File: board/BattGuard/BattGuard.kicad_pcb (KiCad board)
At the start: 4 copper layers, 160 x 80 mm, 160 parts, among them J1 OQ0271510000G, J10 Conn_01x01_Pin, J11 Conn_01x01_Pin, J12 Conn_01x01_Pin, J13 Conn_01x01_Pin, J15 Conn_01x01_Pin, J17 S5B-XH-A, J18 FAN1 5V, J19 FAN2 5V, J2 Barrel_Jack, J3 Conn_01x22_Pin, J4 Conn_01x22_Pin, J5 Conn_01x02_Pin(xt60), J6 OLED DISPLAY, J8 GSB4111312HR, J9 Conn_01x01_Pin, Q1 SIR680LDP-T1-RE3, Q2 SIR680LDP-T1-RE3, Q3 SIR680LDP-T1-RE3, Q4 SIR680LDP-T1-RE3, Q5 Q_PMOS_DGS, Q7 AO3401A, Q8 2N7002, SW1 SW_Push, SW2 SW_Push, U1 BQ25756ERRVR, U2 LMR51420XDDCR, U3 MCP45HV51-ST, U4 INA226, U5 LM317_TO3, U6 TLV76133KVUR, U7 TLV61047DDC

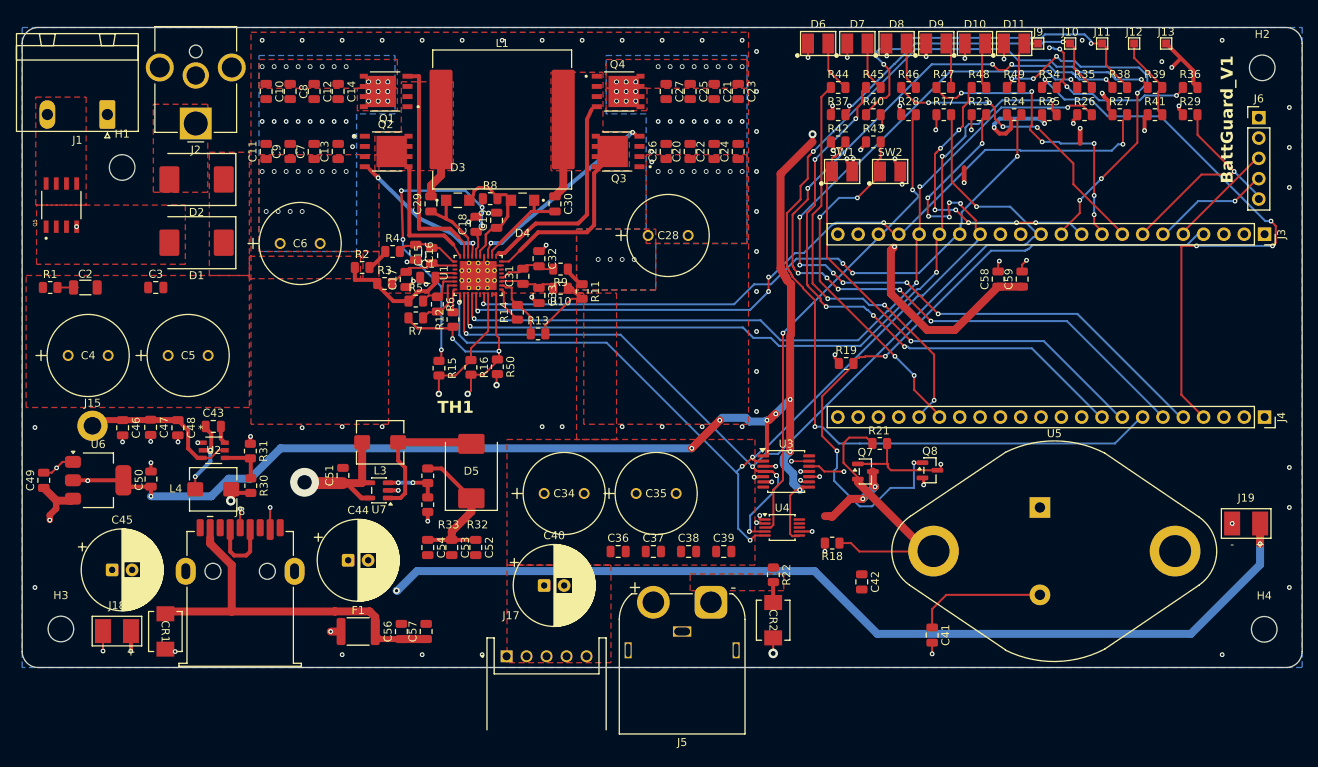
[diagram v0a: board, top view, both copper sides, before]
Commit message: 10.30.2026 updated
updated capicator footprints, cleaned up and routed 12v charge circuit section, updated clearance rules for pad clearnce issues.
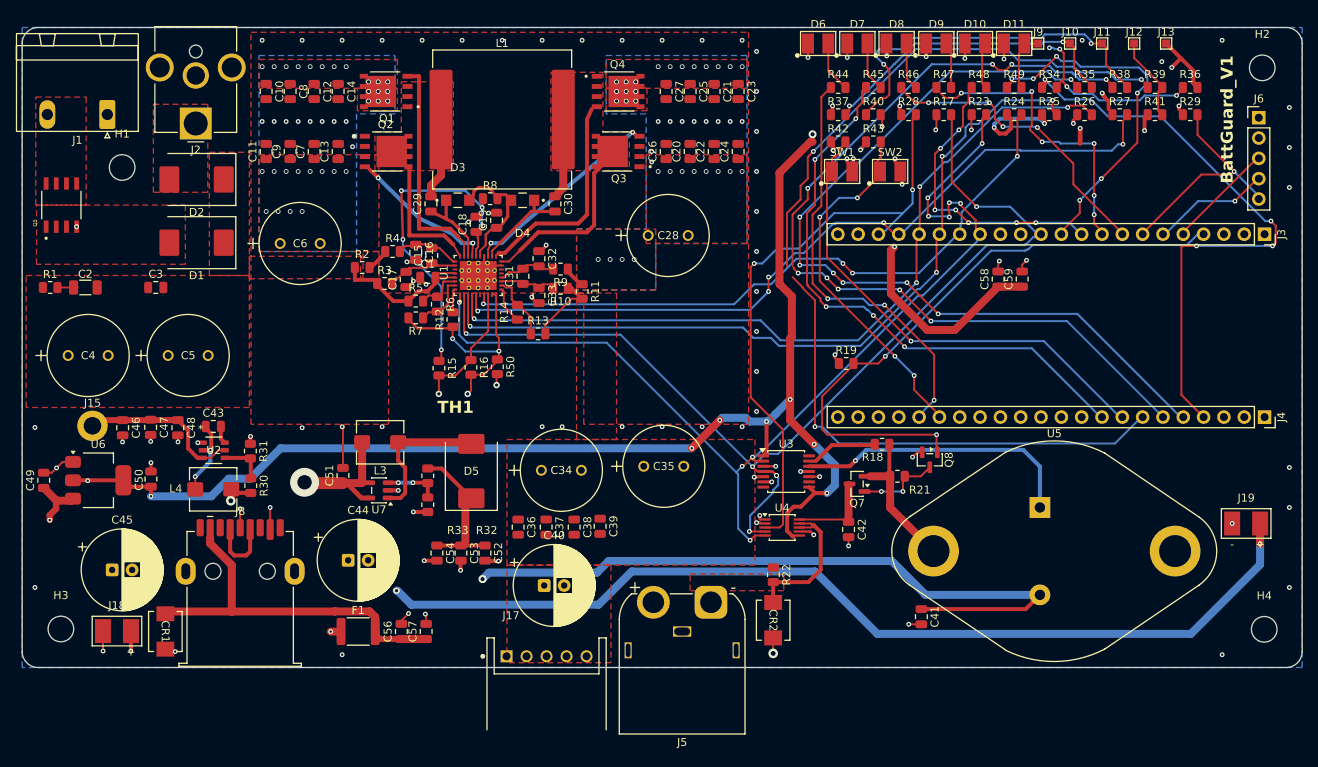
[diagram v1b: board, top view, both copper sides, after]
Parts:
- moved C39 15.8 mm to (172.2, 112.3), turned to -90 degrees
- moved C38 14.6 mm to (169.0, 112.5), turned to -90 degrees
- moved R18 13.8 mm to (207.5, 102.1)
- moved C37 13.7 mm to (165.5, 112.5), turned to -90 degrees
- moved C36 12.9 mm to (162.0, 112.5), turned to -90 degrees
- moved C42 6.75 mm to (203.3, 112.8)
- moved R21 4.66 mm to (209.4, 106.1)
- moved C35 3.53 mm to (177.7, 104.8)
- moved C34 2.92 mm to (164.9, 105.3)
- moved C41 2.67 mm to (212.4, 123.7)
- moved Q7 1.87 mm to (204.4, 107.0), turned to 180 degrees
- moved C52 1.35 mm to (157.8, 115.7)
- moved C53 1.35 mm to (154.8, 115.7)
- moved C54 1.35 mm to (151.8, 115.7)
- moved Q8 1.31 mm to (213.4, 104.0), turned to -90 degrees
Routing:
- net /+18.5V: track 35.7 -> 106.2 mm, vias 0 -> 1
- net +BATT: track 4.37 -> 20.6 mm
- net /GPIO14: track 58.3 -> 74.3 mm
- net Net-(Q7-S): track 64.9 -> 49.6 mm
- net GND: track 55.3 -> 68.0 mm, vias 117 -> 120
- net Net-(U3-P0A): track 17.5 -> 9.10 mm, vias 2 -> 0
- net Net-(Q7-G): track 16.1 -> 9.68 mm, vias 1 -> 2
- net +3V3: track 190.0 -> 195.9 mm, vias 24 -> 23
- net /GPIO4: track 82.4 -> 77.1 mm, vias 3 -> 2
- net /Vsystem: track 113.0 -> 109.1 mm
- net /GPIO41: track 128.7 -> 127.2 mm
- net +5V: track 164.2 -> 165.6 mm
- net Net-(Q7-D): track 9.84 -> 11.1 mm, vias 2 -> 0

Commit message: 10.30.2026 fixed capictor routing, 18.5 feed line setup correctly 12v charge circuit done and cleaned up
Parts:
- moved C58 26.2 mm to (243.5, 66.5), turned to -90 degrees
- moved C59 21.6 mm to (240.5, 66.5), turned to -90 degrees
- moved C42 5.71 mm to (203.0, 118.5)
- moved C36 0.81 mm to (162.8, 112.3)
- moved C37 0.81 mm to (166.3, 112.3)
- moved C38 0.81 mm to (169.8, 112.3)
- moved C39 0.81 mm to (173.1, 112.2)
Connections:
- C58 pad 1: +5V -> +3V3
- C59 pad 1: +5V -> +3V3
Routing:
- net +5V: track 165.6 -> 139.2 mm, vias 7 -> 6
- net Net-(Q7-D): track 11.1 -> 26.8 mm
- net /+18.5V: track 106.2 -> 118.2 mm, vias 1 -> 8
- net GND: track 68.0 -> 78.6 mm, vias 120 -> 125
- net /GPIO9: track 127.4 -> 121.9 mm, vias 10 -> 6
- net +3V3: track 195.9 -> 200.4 mm, vias 23 -> 25
- net +BATT: track 20.6 -> 22.6 mm, vias 0 -> 1
- net Net-(J9-Pin_1): track 23.3 -> 25.3 mm, vias 4 -> 2
- net /GPIO41: track 127.2 -> 128.7 mm
- added copper zone on F.Cu, net /+18.5V

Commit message: 10.30.2026 rev 1
all traces routed, time to go through shivams checklist
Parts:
- R50: value 0 -> NetTie; footprint Resistor_SMD:R_0805_2012Metric -> TeamLib:NetTie_AGND_EP
- moved R50 9.48 mm to (158.8, 83.0), turned to 0 degrees
- moved C29 1.05 mm to (151.1, 73.1)
- moved C30 0.81 mm to (166.7, 72.8), turned to 180 degrees
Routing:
- net /SW1: track 29.2 -> 38.2 mm, vias 0 -> 2
- net /SW2: track 33.7 -> 42.3 mm, vias 0 -> 2
- net /LODRV2: track 24.9 -> 29.6 mm
- net Net-(U1-DRV_SUP): track 10.3 -> 14.5 mm
- net Net-(U1-SRN): track 4.99 -> 6.88 mm
- net GND: track 78.6 -> 77.1 mm, vias 125 -> 124
- net /LODRV1: track 18.0 -> 19.2 mm
- net /REGN: track 40.3 -> 41.1 mm
- net /BTST2: track 12.0 -> 11.4 mm
- net /HIDRV2: vias 0 -> 2
- net /HIDRV1: vias 0 -> 2

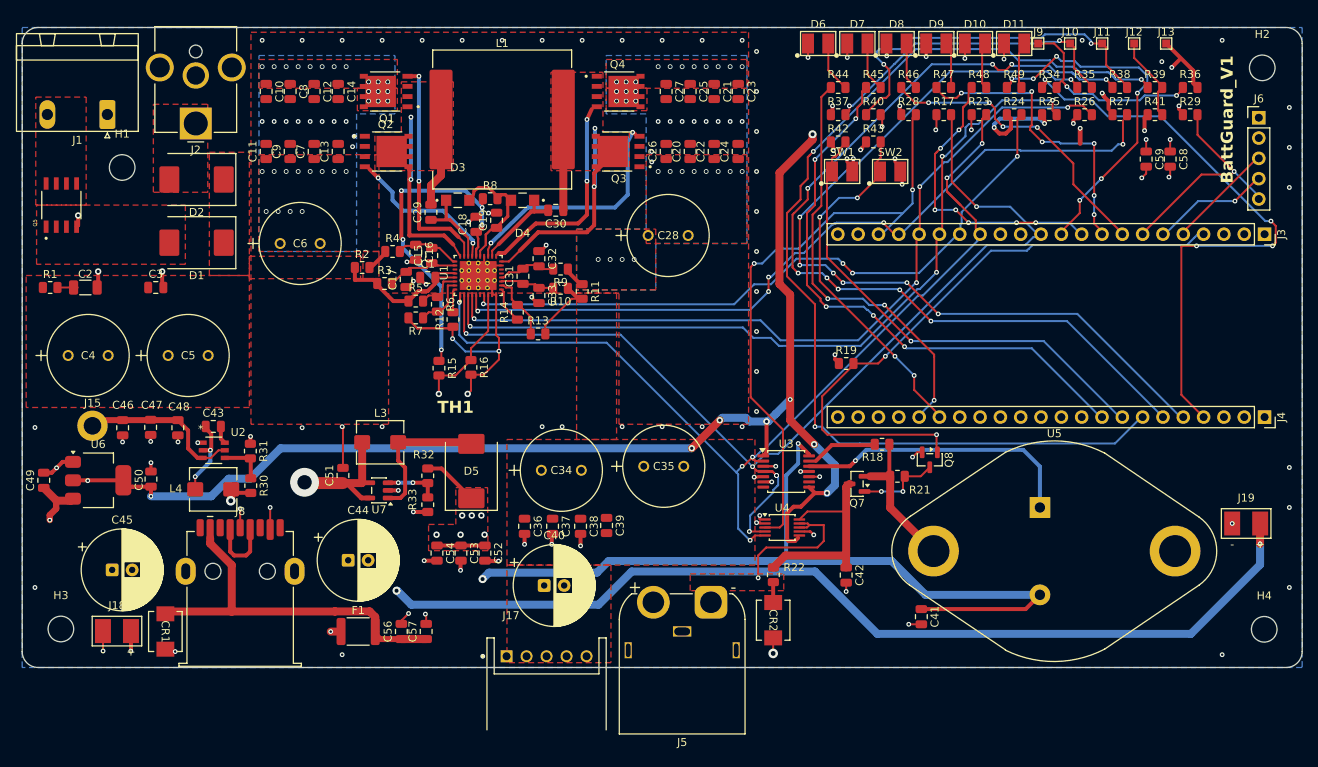
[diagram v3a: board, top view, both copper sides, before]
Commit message: Trace Cleaning/Straigtening SilkScreen Placement and Sizing
Throughout most of the board trace routing has been straightened out where possible. Silkscreen that overlapped in tight areas were resized, and most IC silkscreens labels were moved to nearby its Pin 1.
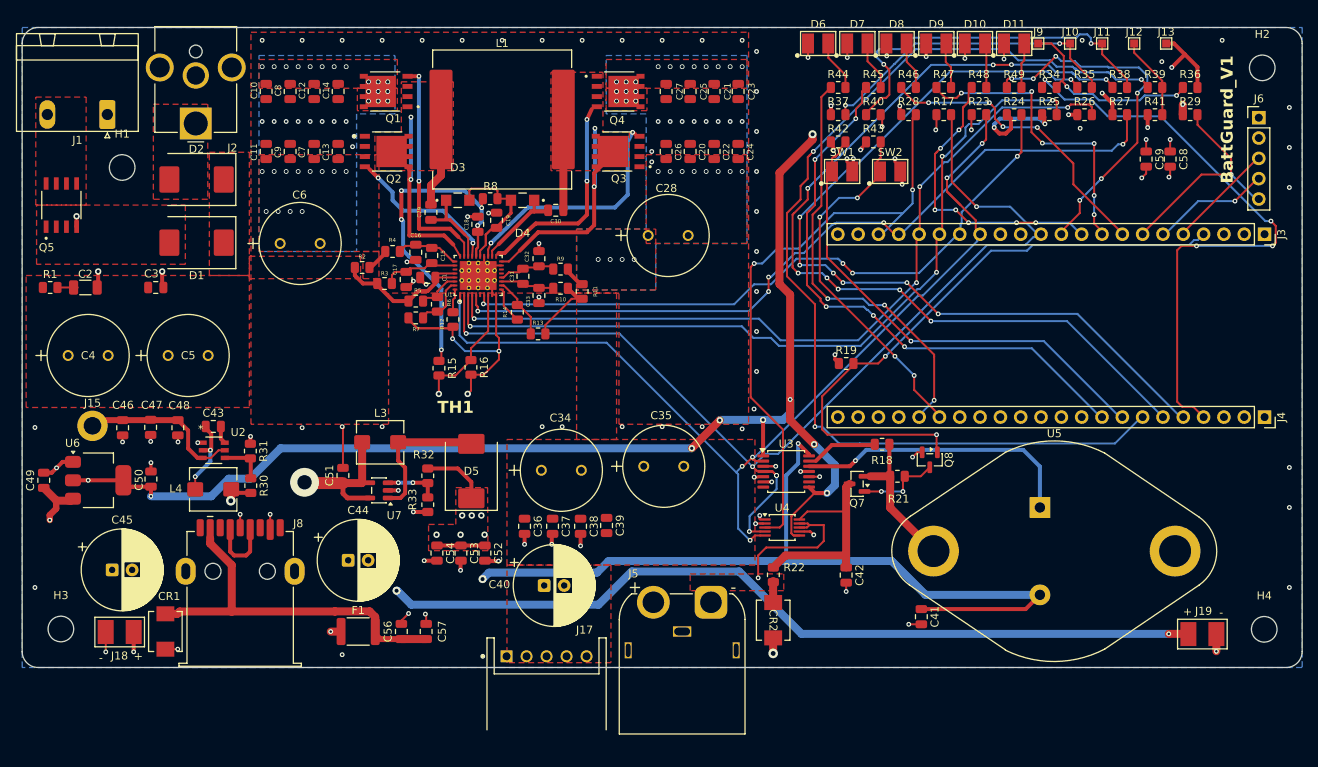
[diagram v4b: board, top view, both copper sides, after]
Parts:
- moved J19 14.9 mm to (247.5, 125.8), turned to 0 degrees
- moved J18 0.36 mm to (112.2, 125.6)
- moved C18 0.20 mm to (156.9, 74.6)
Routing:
- net +5V: track 139.2 -> 123.0 mm
- net +3V3: track 200.2 -> 203.8 mm
- net Net-(U1-ACP): track 7.34 -> 9.81 mm
- net Net-(U1-DRV_SUP): track 14.5 -> 15.8 mm
- net /GPIO13: track 95.6 -> 96.8 mm
- net Net-(D11-A): track 4.43 -> 5.65 mm
- net /+18.5V: track 118.2 -> 119.4 mm
- net /GPIO1: track 74.3 -> 75.5 mm
- net GND: track 77.1 -> 78.2 mm, vias 124 -> 123
- net Net-(D10-A): track 4.51 -> 5.57 mm
- net /GPIO12: track 98.9 -> 99.9 mm
- net Net-(U1-ACUV): track 4.49 -> 5.41 mm
- net /GPIO5: track 11.8 -> 12.7 mm
- net /Vsystem: track 109.1 -> 109.9 mm
- net Net-(U1-ACN): track 6.67 -> 7.35 mm
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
